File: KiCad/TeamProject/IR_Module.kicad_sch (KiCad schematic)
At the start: 15 parts, among them U1 MCP6294, U2 LM339AN

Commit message: Kicad Update
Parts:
- removed U2: LM339AN, symbol ME218_BaseLib:LM339AN
- renumbered C1 to C, R2 to R, R3 to R, R7 to R, Rpu to R, R9 to R, R1 to R, R5 to R, R4 to R, U1 to U
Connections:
- net at R.1, R.2: now also U.3 (+); no longer U.12 (+)
- new net: R.1, U.1, U.2 (-)
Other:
- moved on the sheet: C, UA

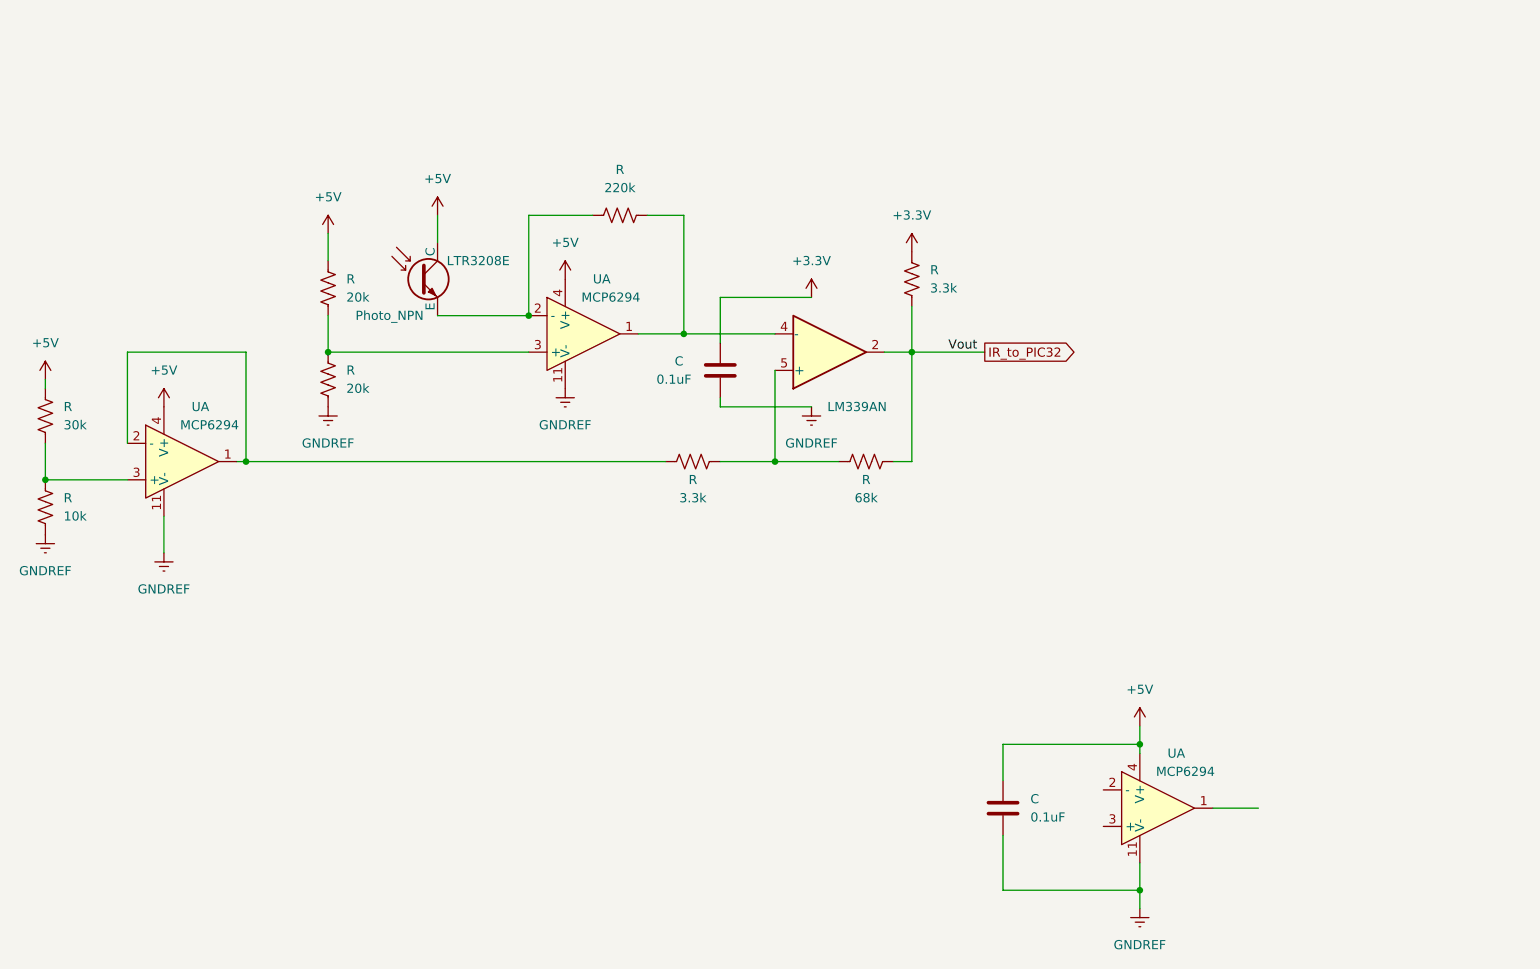
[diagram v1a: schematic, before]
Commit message: change Pin of SPI
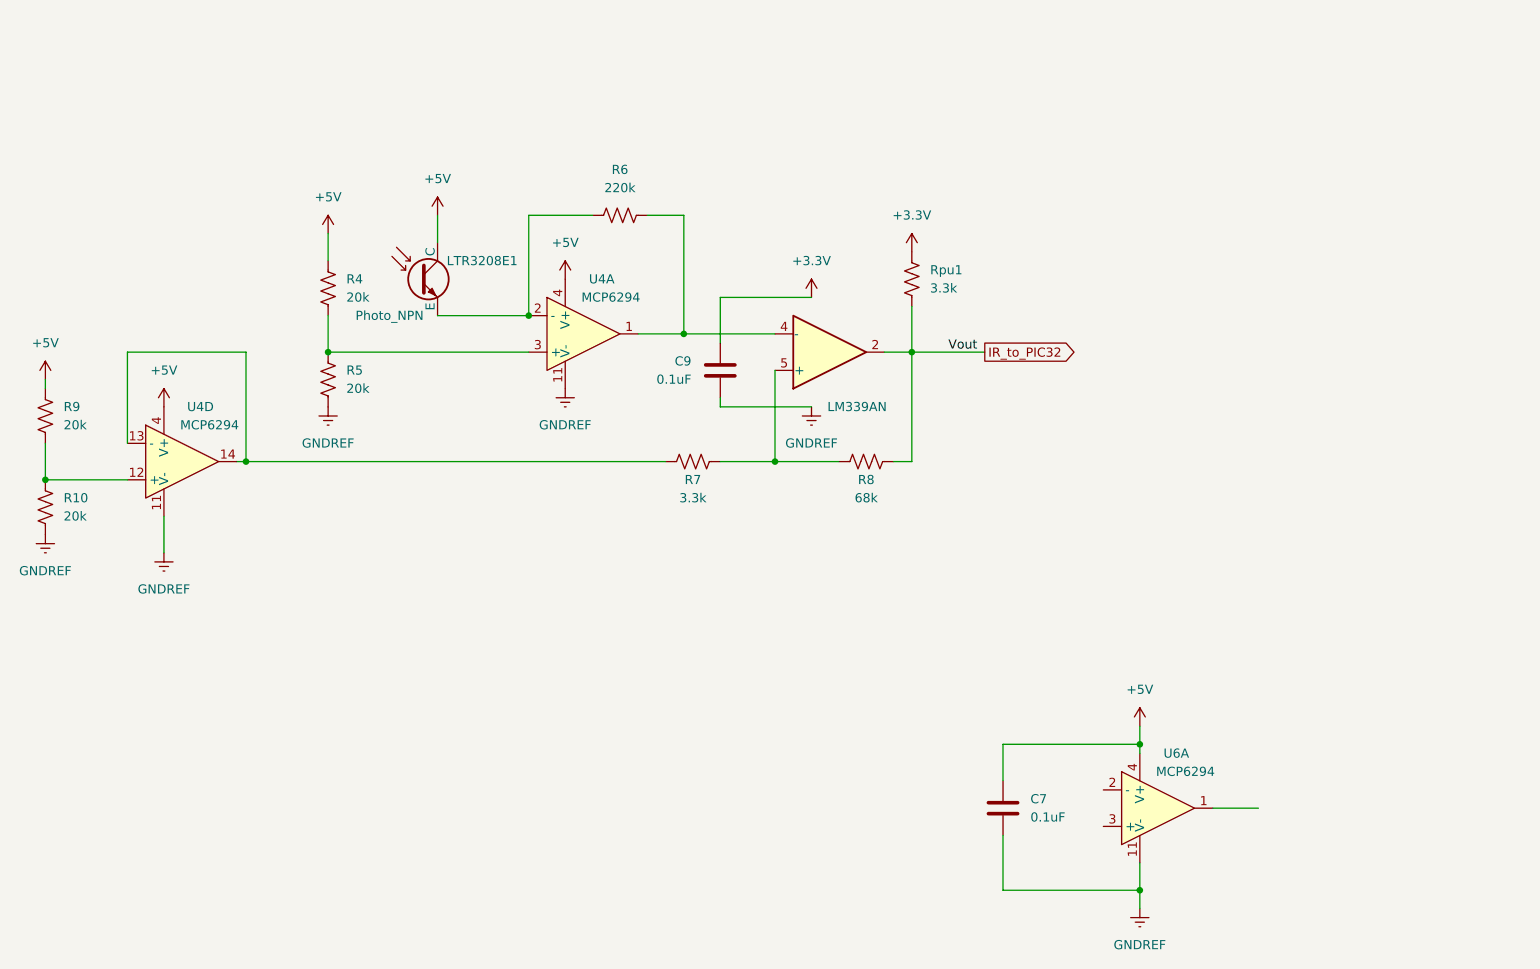
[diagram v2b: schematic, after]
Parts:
- R10: renamed from R; value 10k -> 20k
- R9: renamed from R; value 30k -> 20k
- renumbered C to C7, C to C9, LTR3208E to LTR3208E1, R to R4, R to R5, R to R6, R to R7, R to R8, R to Rpu1, U to U4, U2 to U5, U to U6
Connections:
- net at R10.2, R9.1: now also U4.12 (+); no longer U4.3 (+)
- new net: R7.1, U4.13 (-), U4.14
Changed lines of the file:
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@@
 		(on_board yes)
 		(dnp no)
-		(property "Reference" "C"
+		(property "Reference" "C9"
 			(at 138.43 82.55 0)
 			(effects
@@
 		(on_board yes)
 		(dnp no)
-		(property "Reference" "R"
+		(property "Reference" "R7"
 			(at 140.97 99.06 90)
 			(effects
@@
 		(dnp no)
 		(fields_autoplaced yes)
-		(property "Reference" "#PWR?"
+		(property "Reference" "#PWR09"
 			(at 90.17 95.25 0)
 			(effects
@@
 		(on_board yes)
 		(dnp no)
-		(property "Reference" "R"
+		(property "Reference" "R8"
 			(at 165.1 99.06 90)
 			(effects
@@
 		(dnp no)
 		(fields_autoplaced yes)
-		(property "Reference" "R"
+		(property "Reference" "R9"
 			(at 53.34 88.8999 0)
 			(effects
@@
 			)
 		)
-		(property "Value" "30k"
+		(property "Value" "20k"
 			(at 53.34 91.4399 0)
 			(effects
@@
 		(dnp no)
 		(fields_autoplaced yes)
-		(property "Reference" "#PWR?"
+		(property "Reference" "#PWR029"
 			(at 157.48 77.47 0)
 			(effects
@@
 		(dnp no)
 		(fields_autoplaced yes)
-		(property "Reference" "#PWR?"
+		(property "Reference" "#PWR032"
 			(at 67.31 115.57 0)
 			(effects
@@
 		(dnp no)
 		(fields_autoplaced yes)
-		(property "Reference" "#PWR?"
+		(property "Reference" "#PWR022"
 			(at 105.41 66.04 0)
 			(effects
@@
 		(dnp no)
 		(fields_autoplaced yes)
-		(property "Reference" "#PWR?"
+		(property "Reference" "#PWR023"
 			(at 123.19 74.93 0)
 			(effects
@@
 		(dnp no)
 		(fields_autoplaced yes)
-		(property "Reference" "C"
+		(property "Reference" "C7"
 			(at 187.96 143.5099 0)
 			(effects
@@
 		(dnp no)
 		(fields_autoplaced yes)
-		(property "Reference" "#PWR?"
+		(property "Reference" "#PWR030"
 			(at 157.48 95.25 0)
 			(effects
@@
 		(dnp no)
 		(fields_autoplaced yes)
-		(property "Reference" "#PWR?"
+		(property "Reference" "#PWR024"
 			(at 123.19 92.71 0)
 			(effects
@@
 		(dnp no)
 		(fields_autoplaced yes)
-		(property "Reference" "#PWR?"
+		(property "Reference" "#PWR021"
 			(at 50.8 113.03 0)
 			(effects
@@
 		(dnp no)
 		(fields_autoplaced yes)
-		(property "Reference" "#PWR?"
+		(property "Reference" "#PWR031"
 			(at 67.31 92.71 0)
 			(effects
@@
 		(lib_id "ME218_BaseLib:MCP6294")
 		(at 69.85 96.52 0)
-		(unit 1)
-		(exclude_from_sim no)
-		(in_bom yes)
-		(on_board yes)
-		(dnp no)
-		(property "Reference" "U"
+		(unit 4)
+		(exclude_from_sim no)
+		(in_bom yes)
+		(on_board yes)
+		(dnp no)
+		(property "Reference" "U4"
 			(at 72.39 88.9 0)
 			(effects
@@
 		(dnp no)
 		(fields_autoplaced yes)
-		(property "Reference" "#PWR?"
+		(property "Reference" "#PWR020"
 			(at 50.8 88.9 0)
 			(effects
@@
 		(dnp no)
 		(fields_autoplaced yes)
-		(property "Reference" "R"
+		(property "Reference" "Rpu1"
 			(at 173.99 69.8499 0)
 			(effects
@@
 		(on_board yes)
 		(dnp no)
-		(property "Reference" "LTR3208E?"
+		(property "Reference" "LTR3208E1"
 			(at 106.68 68.58 0)
 			(effects
@@
 		(dnp no)
 		(fields_autoplaced yes)
-		(property "Reference" "R"
+		(property "Reference" "R10"
 			(at 53.34 101.5999 0)
 			(effects
@@
 			)
 		)
-		(property "Value" "10k"
+		(property "Value" "20k"
 			(at 53.34 104.1399 0)
 			(effects
@@
 		(dnp no)
 		(fields_autoplaced yes)
-		(property "Reference" "R"
+		(property "Reference" "R6"
 			(at 130.81 55.88 90)
 			(effects
@@
 		(on_board yes)
 		(dnp no)
-		(property "Reference" "U"
+		(property "Reference" "U4"
 			(at 128.27 71.12 0)
 			(effects
@@
 		(dnp no)
 		(fields_autoplaced yes)
-		(property "Reference" "R"
+		(property "Reference" "R5"
 			(at 92.71 83.8199 0)
 			(effects
@@
 		(dnp no)
 		(fields_autoplaced yes)
-		(property "Reference" "#PWR?"
+		(property "Reference" "#PWR027"
 			(at 171.45 71.12 0)
 			(effects
@@
 		(dnp no)
 		(fields_autoplaced yes)
-		(property "Reference" "#PWR?"
+		(property "Reference" "#PWR025"
 			(at 203.2 137.16 0)
 			(effects
@@
 		(dnp no)
 		(fields_autoplaced yes)
-		(property "Reference" "#PWR?"
+		(property "Reference" "#PWR026"
 			(at 203.2 165.1 0)
 			(effects
@@
 		(on_board yes)
 		(dnp no)
-		(property "Reference" "U"
+		(property "Reference" "U6"
 			(at 208.28 137.16 0)
 			(effects
@@
 		(on_board yes)
 		(dnp no)
-		(property "Reference" "U?"
+		(property "Reference" "U5"
 			(at 153.67 104.14 0)
 			(effects
@@
 		(dnp no)
 		(fields_autoplaced yes)
-		(property "Reference" "#PWR?"
+		(property "Reference" "#PWR08"
 			(at 90.17 68.58 0)
 			(effects
@@
 		(dnp no)
 		(fields_autoplaced yes)
-		(property "Reference" "R"
+		(property "Reference" "R4"
 			(at 92.71 71.1199 0)
 			(effects

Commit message: Update IR module schematics
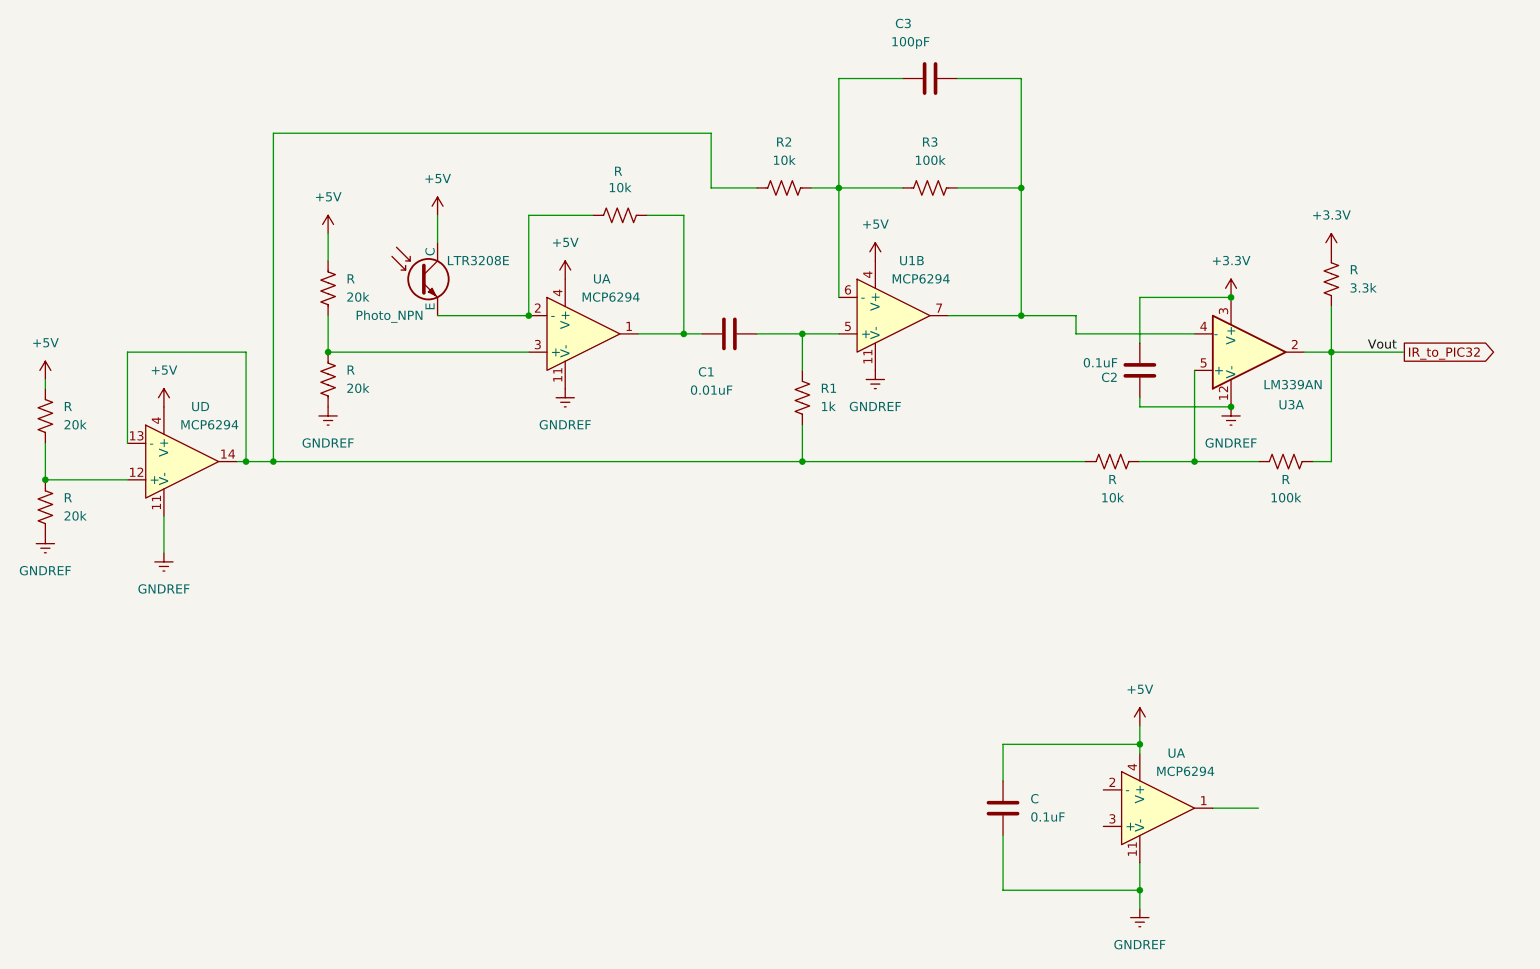
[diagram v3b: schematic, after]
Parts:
- removed C9: 0.1uF, symbol ME218_BaseLib:Cap
- removed U5: LM339AN, symbol ME218_BaseLib:LM339AN
- added C1: 0.01uF, symbol ME218_BaseLib:Cap
- added C2: 0.1uF, symbol ME218_BaseLib:Cap
- added C3: 100pF, symbol ME218_BaseLib:Cap
- added R1: 1k, symbol ME218_BaseLib:Res1
- added R2: 10k, symbol ME218_BaseLib:Res1
- added R3: 100k, symbol ME218_BaseLib:Res1
- added U1: MCP6294, symbol ME218_BaseLib:MCP6294
- added U2, U3: LM339AN, symbol ME218_BaseLib:LM339AN
- R: renamed from R7; value 3.3k -> 10k
- R: renamed from R8; value 68k -> 100k
- R: renamed from R6; value 220k -> 10k
- renumbered C7 to C, LTR3208E1 to LTR3208E, R9 to R, Rpu1 to R, R10 to R, R5 to R, R4 to R, U4 to U, U6 to U
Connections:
- net +3.3V: now also C2.1, U2.3 (V+)
- net +5V: now also U1.4 (V+)
- net GNDREF: now also C2.2, U1.11 (V-), U2.12 (V-)
- net IR_to_PIC32: now also U3.2
- net at R.1, U.13 (-), U.14: now also R1.1, R2.1
- net at R.1, R.2: now also U3.5 (+)
- net at R.2, U.1: now also C1.2
- new net: C1.1, R1.2, U1.5 (+)
- new net: C3.2, R2.2, R3.1, U1.6 (-)
- new net: C3.1, R3.2, U1.7, U3.4 (-)
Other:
- moved on the sheet: R

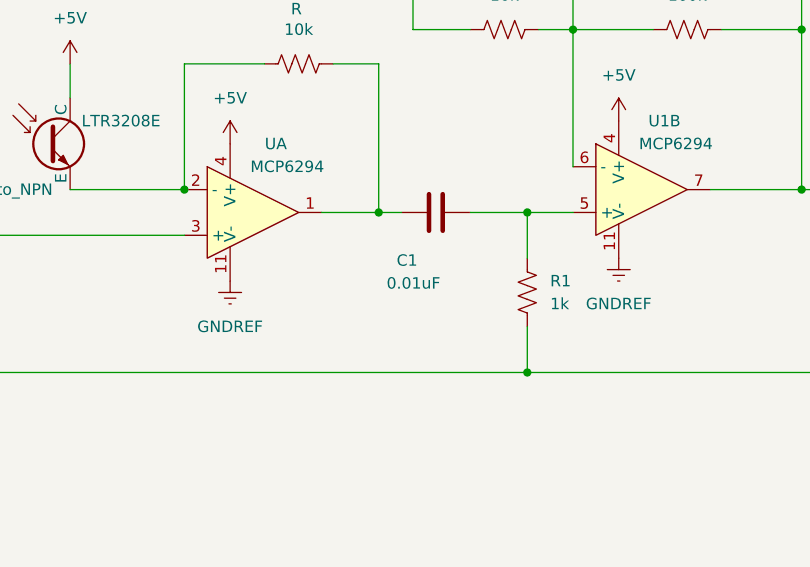
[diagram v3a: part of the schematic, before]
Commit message: Update IR detection RC choosing
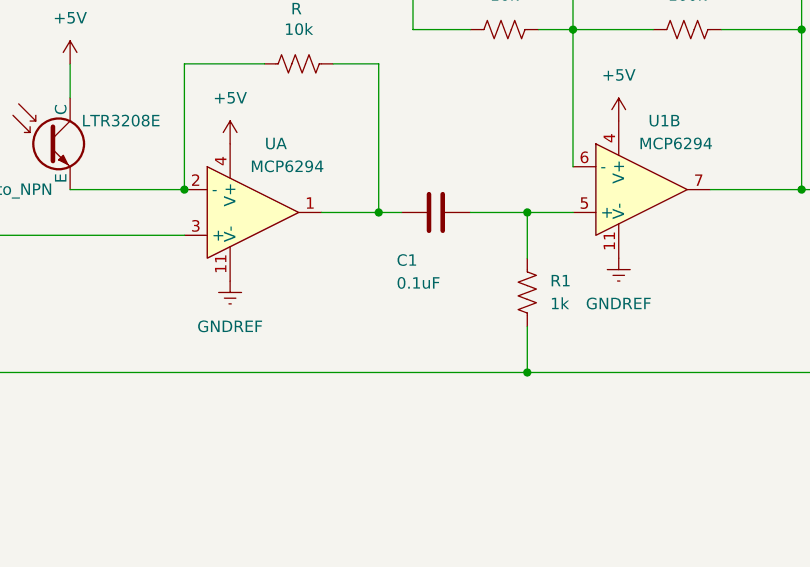
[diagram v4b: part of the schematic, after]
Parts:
- C1: value 0.01uF -> 0.1uF
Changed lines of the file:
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@@
 			)
 		)
-		(property "Value" "0.01uF"
+		(property "Value" "0.1uF"
 			(at 146.558 86.614 90)
 			(effects

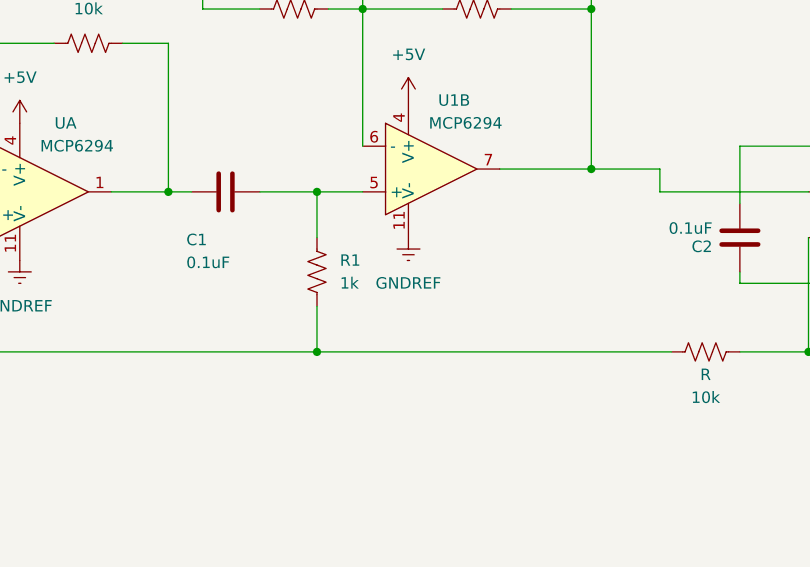
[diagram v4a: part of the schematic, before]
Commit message: Update calculated and tested capacitor and resistor values for beacon detection circuit
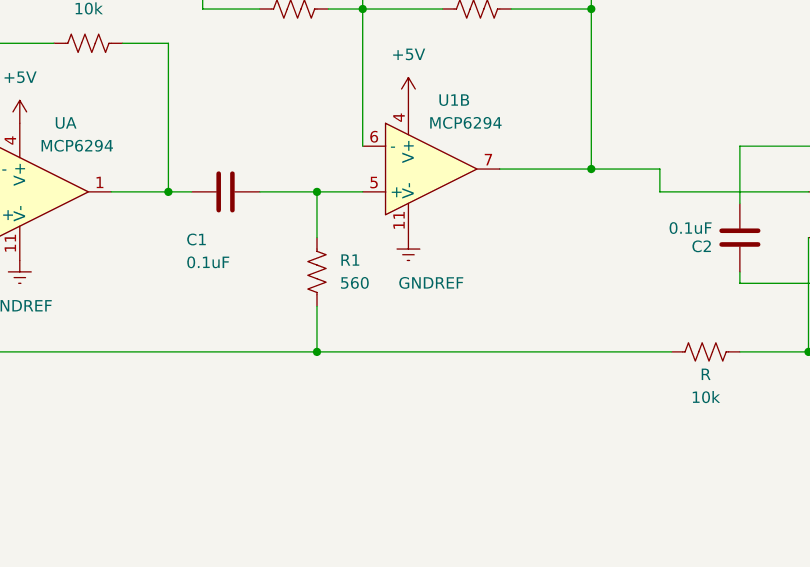
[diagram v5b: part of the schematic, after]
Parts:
- R1: value 1k -> 560
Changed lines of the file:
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@@
 		(on_board yes)
 		(dnp no)
-		(fields_autoplaced yes)
 		(property "Reference" "#PWR02"
 			(at 166.37 90.17 0)
@@
 		)
 		(property "Value" "GNDREF"
-			(at 166.37 88.9 0)
+			(at 168.91 88.9 0)
 			(effects
 				(font
@@
 			)
 		)
-		(property "Value" "1k"
+		(property "Value" "560"
 			(at 158.75 88.8999 0)
 			(effects
